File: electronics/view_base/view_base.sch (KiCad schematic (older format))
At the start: 103 parts, among them J1 BLDC, J2 USB_C_Receptacle_USB2.0, J3 LCD, J4 A, J5 B, Q1 MMBT4403, Q2 UMH3N, U1 MT6701-CT, U2 T-Micro32_Plus, U3 CH340C, U4 HX711, U5 TMC6300, U6 AP2114HA-3.3, U7 SN74LV1T34DBV, U8 VEML7700

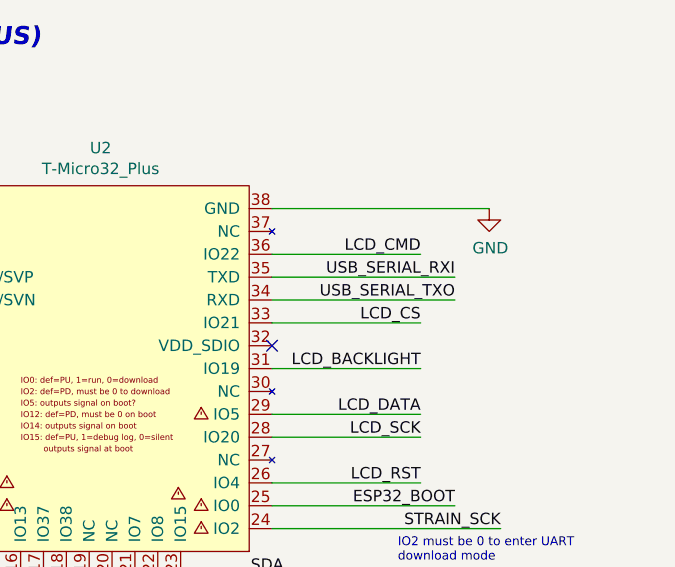
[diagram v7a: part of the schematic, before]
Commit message: Add testpoints for RX and TX
Updates #14
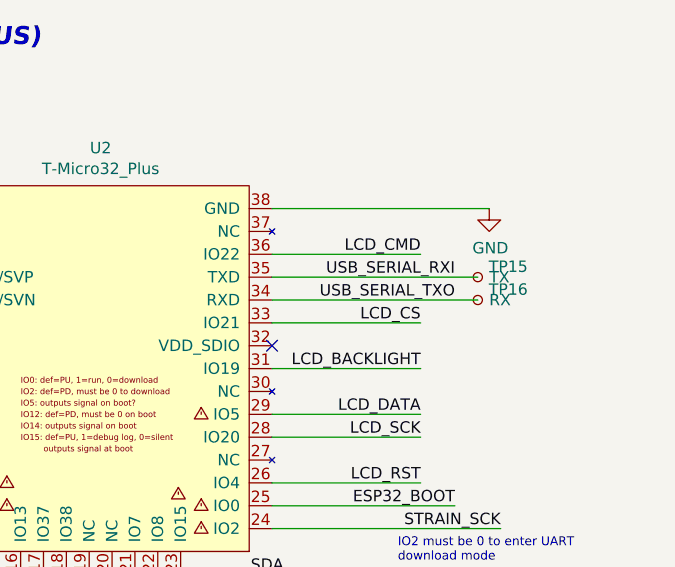
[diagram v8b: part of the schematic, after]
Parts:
- added TP15: TX, Modified:TestPoint_Pad_D2.0mm_ValueSilk, symbol Connector:TestPoint_Small
- added TP16: RX, Modified:TestPoint_Pad_D2.0mm_ValueSilk, symbol Connector:TestPoint_Small
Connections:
- net USB_SERIAL_RXI: now also TP15.1
- net USB_SERIAL_TXO: now also TP16.1
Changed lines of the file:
@@
 Text Label 15700 1700 2    50   ~ 0
 USB_SERIAL_TXO
-Wire Wire Line
-	15700 1700 14900 1700
-Wire Wire Line
-	14900 1600 15700 1600
 $Comp
 L Connector_Generic:Conn_01x08 J3
@@
 $EndComp
 NoConn ~ 5800 1850
+$Comp
+L Connector:TestPoint_Small TP15
+U 1 1 62379E81
+P 15800 1600
+F 0 "TP15" H 15848 1646 50  0000 L CNN
+F 1 "TX" H 15850 1600 50  0000 L CNN
+F 2 "Modified:TestPoint_Pad_D2.0mm_ValueSilk" H 16000 1600 50  0001 C CNN
+F 3 "~" H 16000 1600 50  0001 C CNN
+	1    15800 1600
+	1    0    0    -1
+$EndComp
+Wire Wire Line
+	14900 1600 15800 1600
+$Comp
+L Connector:TestPoint_Small TP16
+U 1 1 623A126C
+P 15800 1700
+F 0 "TP16" H 15848 1746 50  0000 L CNN
+F 1 "RX" H 15850 1700 50  0000 L CNN
+F 2 "Modified:TestPoint_Pad_D2.0mm_ValueSilk" H 16000 1700 50  0001 C CNN
+F 3 "~" H 16000 1700 50  0001 C CNN
+	1    15800 1700
+	1    0    0    -1
+$EndComp
+Wire Wire Line
+	14900 1700 15800 1700
 $EndSCHEMATC
